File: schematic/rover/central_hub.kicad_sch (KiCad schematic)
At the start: 8 parts, among them U1 Pico

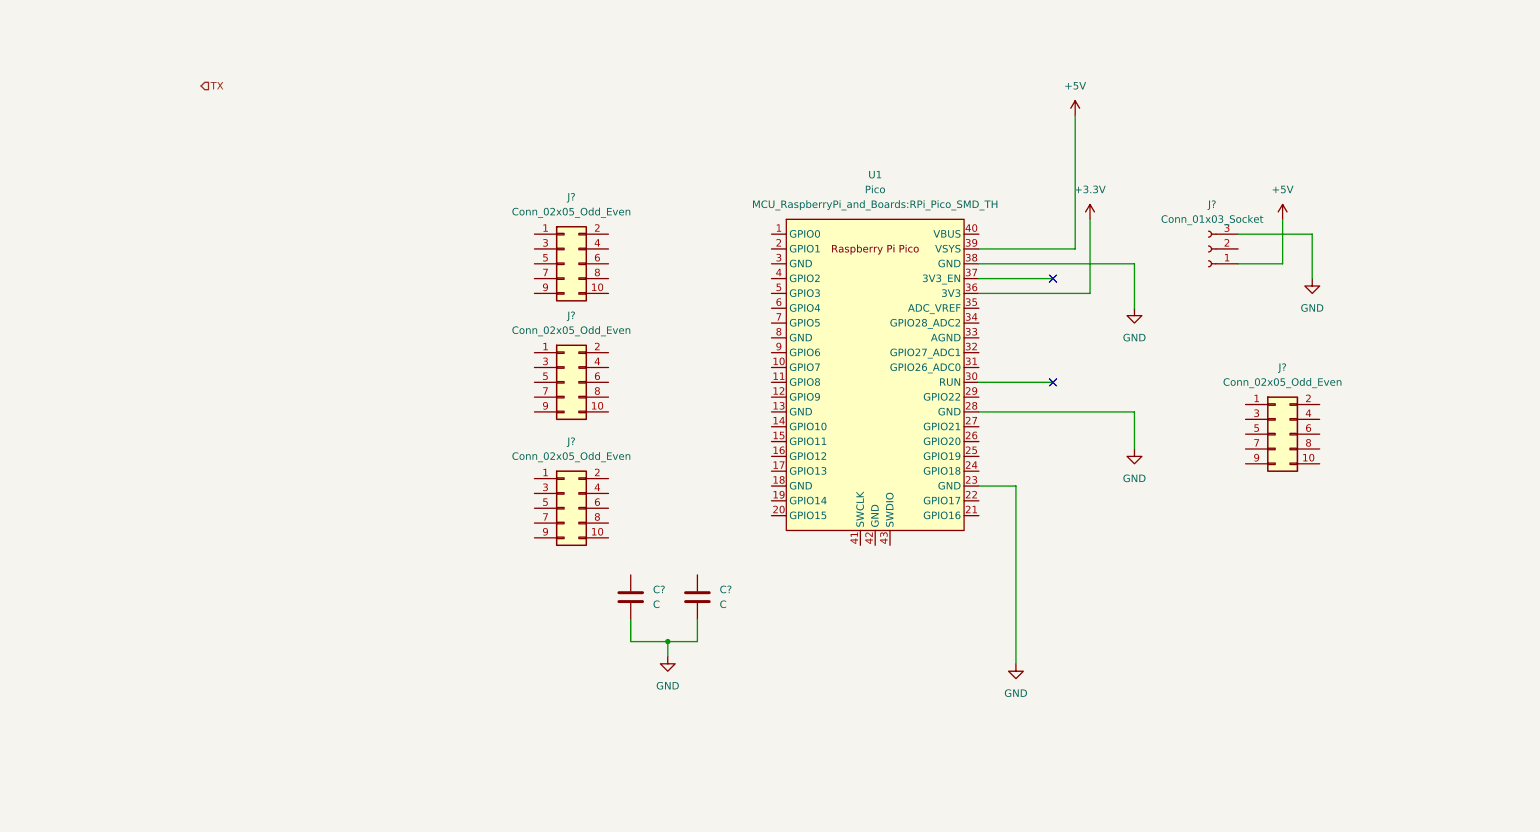
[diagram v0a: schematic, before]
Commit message: Complete Central Hub schematic
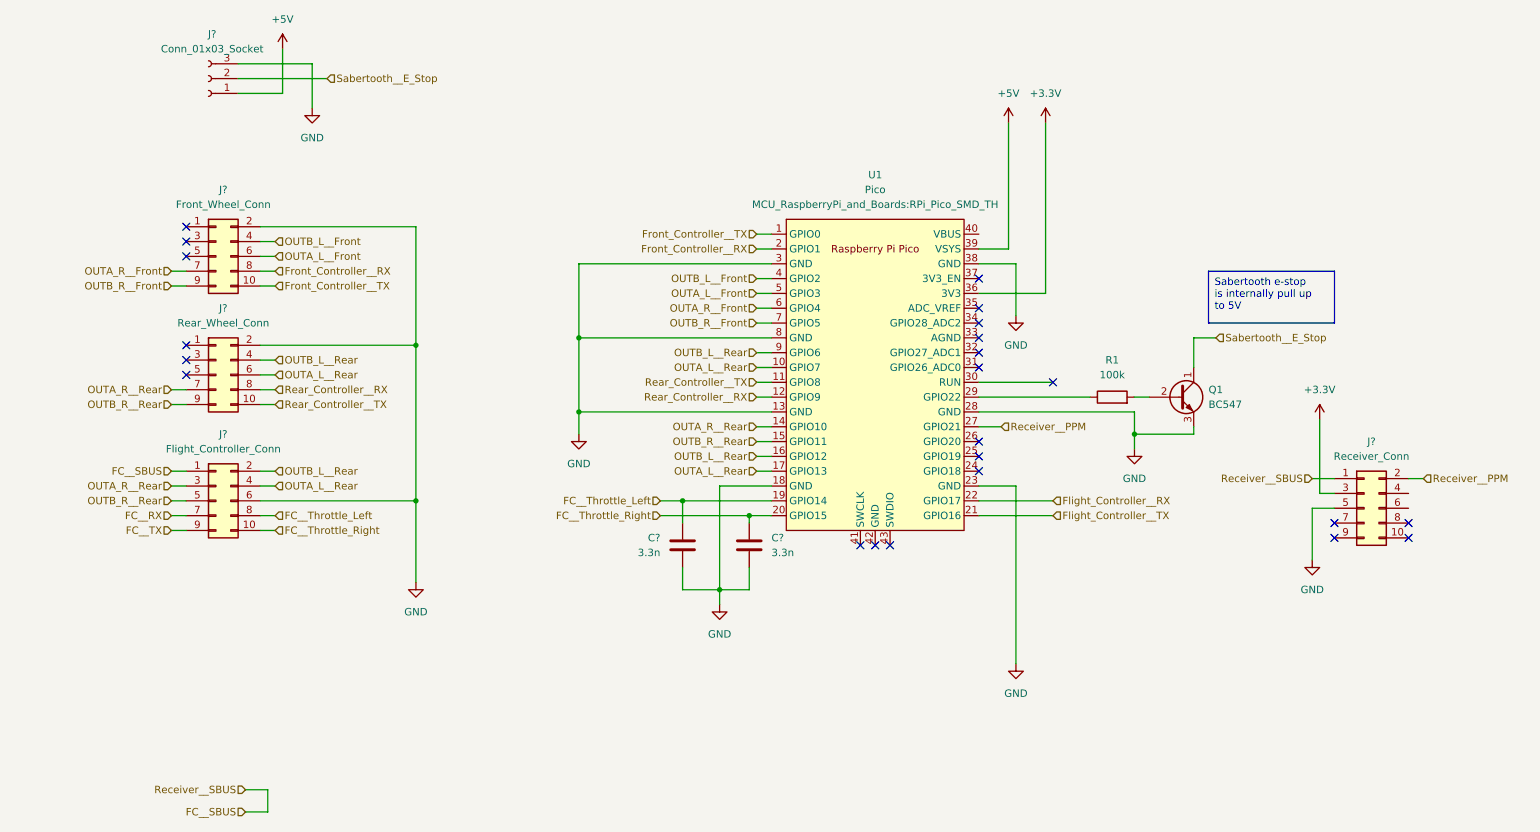
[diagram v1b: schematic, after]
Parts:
- removed C?: C, Capacitor_THT:C_Disc_D7.5mm_W5.0mm_P7.50mm, symbol Device:C
- added C?: 3.3n, Capacitor_THT:C_Disc_D5.0mm_W2.5mm_P5.00mm, symbol Device:C
- added Q1: BC547, Package_TO_SOT_THT:TO-92_Inline, symbol Transistor_BJT:BC547
- added R1: 100k, Resistor_THT:R_Axial_DIN0207_L6.3mm_D2.5mm_P5.08mm_Vertical, symbol Device:R
- C?: value C -> 3.3n; footprint Capacitor_THT:C_Disc_D7.5mm_W5.0mm_P7.50mm -> Capacitor_THT:C_Disc_D5.0mm_W2.5mm_P5.00mm
- J?: value Conn_02x05_Odd_Even -> Receiver_Conn
- J?: value Conn_02x05_Odd_Even -> Rear_Wheel_Conn
- J?: value Conn_02x05_Odd_Even -> Front_Wheel_Conn
- J?: value Conn_02x05_Odd_Even -> Flight_Controller_Conn
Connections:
- net +3.3V: now also J?.3 (Pin_3)
- net GND: now also J?.2 (Pin_2), J?.2 (Pin_2), J?.5 (Pin_5), J?.6 (Pin_6), U1.13 (GND), U1.18 (GND), U1.3 (GND), U1.8 (GND), C?.2, Q1.3 (E)
- net FC__SBUS: now reaches J?.1 (Pin_1)
- net FC__SBUS: now also J?.1 (Pin_1)
- net Receiver__PPM: now reaches J?.2 (Pin_2)
- net Receiver__PPM: now also U1.27 (GPIO21)
- net Sabertooth__E_Stop: now reaches J?.2 (Pin_2)
- net Sabertooth__E_Stop: now also Q1.1 (C)
- net Front_Controller__TX: now reaches U1.1 (GPIO0)
- net Front_Controller__TX: now also J?.10 (Pin_10)
- net OUTA_L__Rear: now reaches U1.10 (GPIO7)
- net OUTA_L__Rear: now also J?.4 (Pin_4), J?.6 (Pin_6), U1.17 (GPIO13)
- net Rear_Controller__TX: now reaches U1.11 (GPIO8)
- net Rear_Controller__TX: now also J?.10 (Pin_10)
- net Rear_Controller__RX: now reaches U1.12 (GPIO9)
- net Rear_Controller__RX: now also J?.8 (Pin_8)
- net OUTA_R__Rear: now reaches U1.14 (GPIO10)
- net OUTA_R__Rear: now also J?.3 (Pin_3), J?.7 (Pin_7)
- net OUTB_R__Rear: now reaches U1.15 (GPIO11)
- net OUTB_R__Rear: now also J?.5 (Pin_5), J?.9 (Pin_9)
- net OUTB_L__Rear: now reaches U1.16 (GPIO12)
- net OUTB_L__Rear: now also J?.2 (Pin_2), J?.4 (Pin_4), U1.9 (GPIO6)
- net FC__Throttle_Left: now reaches U1.19 (GPIO14)
- net FC__Throttle_Left: now also C?.1, J?.8 (Pin_8)
- net Front_Controller__RX: now reaches U1.2 (GPIO1)
- net Front_Controller__RX: now also J?.8 (Pin_8)
- net FC__Throttle_Right: now reaches U1.20 (GPIO15)
- net FC__Throttle_Right: now also J?.10 (Pin_10), C?.1
- net Flight_Controller__TX: now reaches U1.21 (GPIO16)
- net Flight_Controller__RX: now reaches U1.22 (GPIO17)
- net at U1.29 (GPIO22): now also R1.1
- net OUTB_L__Front: now reaches U1.4 (GPIO2)
- net OUTB_L__Front: now also J?.4 (Pin_4)
- net OUTA_L__Front: now reaches U1.5 (GPIO3)
- net OUTA_L__Front: now also J?.6 (Pin_6)
- net OUTA_R__Front: now reaches U1.6 (GPIO4)
- net OUTA_R__Front: now also J?.7 (Pin_7)
- net OUTB_R__Front: now reaches U1.7 (GPIO5)
- net OUTB_R__Front: now also J?.9 (Pin_9)
- net FC__RX: now reaches J?.7 (Pin_7)
- net FC__TX: now reaches J?.9 (Pin_9)
- new net: Q1.2 (B), R1.2
- no-connect marks 2 -> 23
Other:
- moved on the sheet: C?, J?

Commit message: Update connection between picos
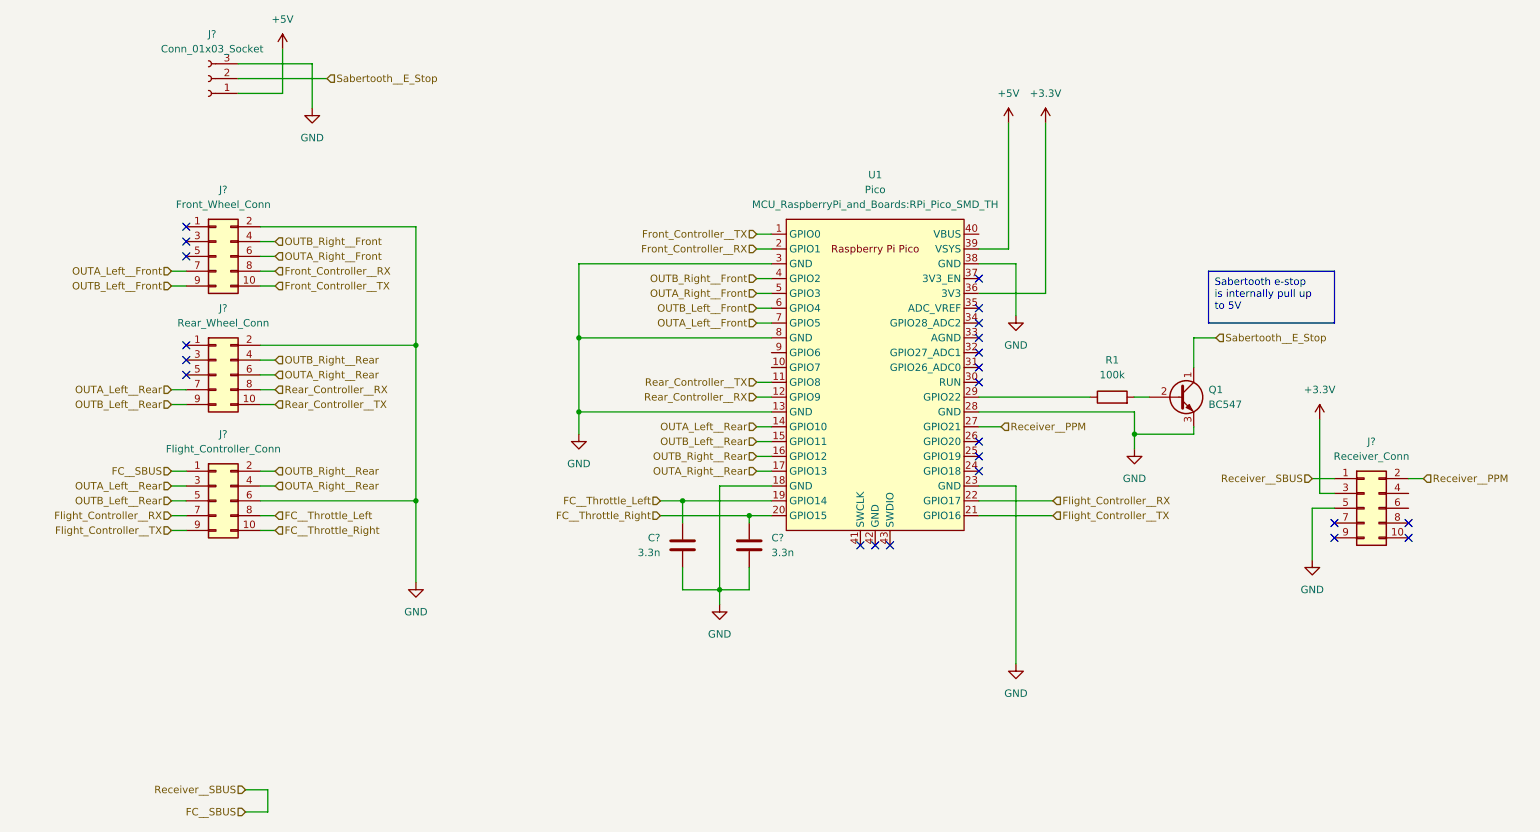
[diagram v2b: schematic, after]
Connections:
- net FC__RX is gone; now on net Flight_Controller__RX: J?.7 (Pin_7)
- net FC__TX is gone; now on net Flight_Controller__TX: J?.9 (Pin_9)
- net OUTA_L__Front renamed OUTA_Right__Front
- net OUTA_L__Rear renamed OUTA_Right__Rear
- net OUTA_Right__Rear: no longer U1.10 (GPIO7)
- net OUTA_R__Front renamed OUTA_Left__Front
- net OUTA_Left__Front: now also U1.7 (GPIO5); no longer U1.6 (GPIO4)
- net OUTA_R__Rear renamed OUTA_Left__Rear
- net OUTB_L__Front renamed OUTB_Right__Front
- net OUTB_L__Rear renamed OUTB_Right__Rear
- net OUTB_Right__Rear: no longer U1.9 (GPIO6)
- net OUTB_R__Front renamed OUTB_Left__Front
- net OUTB_Left__Front: now also U1.6 (GPIO4); no longer U1.7 (GPIO5)
- net OUTB_R__Rear renamed OUTB_Left__Rear
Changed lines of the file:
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@@
   (no_connect (at 238.76 114.3))
   (no_connect (at 41.91 86.36))
-  (no_connect (at 190.5 87.63))
+  (no_connect (at 177.8 87.63))
   (no_connect (at 177.8 77.47))
   (no_connect (at 177.8 85.09))
@@
     (stroke (width 0) (type default))
   )
-  (wire (pts (xy 190.5 87.63) (xy 177.8 87.63))
-    (stroke (width 0) (type default))
-  )
   (wire (pts (xy 204.47 92.71) (xy 204.47 96.52))
     (stroke (width 0) (type default))
@@
     (stroke (width 0) (type default))
   )
-  (wire (pts (xy 139.7 85.09) (xy 142.24 85.09))
-    (stroke (width 0) (type default))
-  )
   (wire (pts (xy 109.22 92.71) (xy 109.22 96.52))
     (stroke (width 0) (type default))
@@
   )
   (wire (pts (xy 138.43 110.49) (xy 138.43 111.76))
-    (stroke (width 0) (type default))
-  )
-  (wire (pts (xy 139.7 82.55) (xy 142.24 82.55))
     (stroke (width 0) (type default))
   )
@@
     (effects (font (size 1.27 1.27)) (justify left top))
   )
-  (hierarchical_label "OUTA_R__Rear" (shape input) (at 139.7 95.25 180) (fields_autoplaced)
-    (effects (font (size 1.27 1.27)) (justify right))
-  )
-  (hierarchical_label "OUTA_L__Front" (shape input) (at 139.7 72.39 180) (fields_autoplaced)
+  (hierarchical_label "OUTA_Left__Rear" (shape input) (at 139.7 95.25 180) (fields_autoplaced)
+    (effects (font (size 1.27 1.27)) (justify right))
+  )
+  (hierarchical_label "OUTA_Right__Front" (shape input) (at 139.7 72.39 180) (fields_autoplaced)
     (effects (font (size 1.27 1.27)) (justify right))
   )
@@
     (effects (font (size 1.27 1.27)) (justify left))
   )
-  (hierarchical_label "OUTB_L__Rear" (shape input) (at 139.7 82.55 180) (fields_autoplaced)
-    (effects (font (size 1.27 1.27)) (justify right))
-  )
-  (hierarchical_label "OUTB_R__Rear" (shape input) (at 39.37 107.95 180) (fields_autoplaced)
+  (hierarchical_label "OUTB_Left__Rear" (shape input) (at 39.37 107.95 180) (fields_autoplaced)
     (effects (font (size 1.27 1.27)) (justify right))
   )
@@
     (effects (font (size 1.27 1.27)) (justify left))
   )
-  (hierarchical_label "OUTA_R__Front" (shape input) (at 39.37 68.58 180) (fields_autoplaced)
-    (effects (font (size 1.27 1.27)) (justify right))
-  )
-  (hierarchical_label "OUTB_R__Front" (shape input) (at 39.37 71.12 180) (fields_autoplaced)
+  (hierarchical_label "OUTA_Left__Front" (shape input) (at 39.37 68.58 180) (fields_autoplaced)
+    (effects (font (size 1.27 1.27)) (justify right))
+  )
+  (hierarchical_label "OUTB_Left__Front" (shape input) (at 39.37 71.12 180) (fields_autoplaced)
     (effects (font (size 1.27 1.27)) (justify right))
   )
@@
     (effects (font (size 1.27 1.27)) (justify left))
   )
-  (hierarchical_label "OUTB_L__Front" (shape input) (at 139.7 69.85 180) (fields_autoplaced)
+  (hierarchical_label "OUTB_Right__Front" (shape input) (at 139.7 69.85 180) (fields_autoplaced)
     (effects (font (size 1.27 1.27)) (justify right))
   )
@@
     (effects (font (size 1.27 1.27)) (justify left))
   )
-  (hierarchical_label "OUTB_L__Rear" (shape input) (at 57.15 102.87 0) (fields_autoplaced)
+  (hierarchical_label "OUTB_Right__Rear" (shape input) (at 57.15 102.87 0) (fields_autoplaced)
     (effects (font (size 1.27 1.27)) (justify left))
   )
@@
     (effects (font (size 1.27 1.27)) (justify right))
   )
-  (hierarchical_label "OUTB_L__Front" (shape input) (at 57.15 63.5 0) (fields_autoplaced)
-    (effects (font (size 1.27 1.27)) (justify left))
-  )
-  (hierarchical_label "OUTA_L__Rear" (shape input) (at 139.7 85.09 180) (fields_autoplaced)
-    (effects (font (size 1.27 1.27)) (justify right))
-  )
-  (hierarchical_label "OUTA_R__Rear" (shape input) (at 39.37 88.9 180) (fields_autoplaced)
+  (hierarchical_label "OUTB_Right__Front" (shape input) (at 57.15 63.5 0) (fields_autoplaced)
+    (effects (font (size 1.27 1.27)) (justify left))
+  )
+  (hierarchical_label "OUTA_Left__Rear" (shape input) (at 39.37 88.9 180) (fields_autoplaced)
     (effects (font (size 1.27 1.27)) (justify right))
   )
@@
     (effects (font (size 1.27 1.27)) (justify left))
   )
-  (hierarchical_label "OUTB_R__Rear" (shape input) (at 139.7 97.79 180) (fields_autoplaced)
+  (hierarchical_label "OUTB_Left__Rear" (shape input) (at 139.7 97.79 180) (fields_autoplaced)
+    (effects (font (size 1.27 1.27)) (justify right))
+  )
+  (hierarchical_label "OUTA_Left__Front" (shape input) (at 139.7 77.47 180) (fields_autoplaced)
     (effects (font (size 1.27 1.27)) (justify right))
   )
@@
     (effects (font (size 1.27 1.27)) (justify left))
   )
-  (hierarchical_label "OUTA_R__Rear" (shape input) (at 39.37 105.41 180) (fields_autoplaced)
-    (effects (font (size 1.27 1.27)) (justify right))
-  )
-  (hierarchical_label "OUTB_R__Front" (shape input) (at 139.7 77.47 180) (fields_autoplaced)
-    (effects (font (size 1.27 1.27)) (justify right))
-  )
-  (hierarchical_label "OUTA_R__Front" (shape input) (at 139.7 74.93 180) (fields_autoplaced)
-    (effects (font (size 1.27 1.27)) (justify right))
-  )
-  (hierarchical_label "FC__RX" (shape input) (at 39.37 110.49 180) (fields_autoplaced)
-    (effects (font (size 1.27 1.27)) (justify right))
-  )
-  (hierarchical_label "OUTB_R__Rear" (shape input) (at 39.37 91.44 180) (fields_autoplaced)
+  (hierarchical_label "OUTA_Left__Rear" (shape input) (at 39.37 105.41 180) (fields_autoplaced)
+    (effects (font (size 1.27 1.27)) (justify right))
+  )
+  (hierarchical_label "Flight_Controller__RX" (shape input) (at 39.37 110.49 180) (fields_autoplaced)
+    (effects (font (size 1.27 1.27)) (justify right))
+  )
+  (hierarchical_label "OUTB_Left__Rear" (shape input) (at 39.37 91.44 180) (fields_autoplaced)
     (effects (font (size 1.27 1.27)) (justify right))
   )
@@
     (effects (font (size 1.27 1.27)) (justify right))
   )
-  (hierarchical_label "OUTA_L__Rear" (shape input) (at 139.7 102.87 180) (fields_autoplaced)
+  (hierarchical_label "OUTA_Right__Rear" (shape input) (at 139.7 102.87 180) (fields_autoplaced)
     (effects (font (size 1.27 1.27)) (justify right))
   )
@@
     (effects (font (size 1.27 1.27)) (justify left))
   )
-  (hierarchical_label "FC__TX" (shape input) (at 39.37 113.03 180) (fields_autoplaced)
+  (hierarchical_label "OUTB_Left__Front" (shape input) (at 139.7 74.93 180) (fields_autoplaced)
+    (effects (font (size 1.27 1.27)) (justify right))
+  )
+  (hierarchical_label "Flight_Controller__TX" (shape input) (at 39.37 113.03 180) (fields_autoplaced)
     (effects (font (size 1.27 1.27)) (justify right))
   )
@@
     (effects (font (size 1.27 1.27)) (justify right))
   )
-  (hierarchical_label "OUTB_L__Rear" (shape input) (at 57.15 83.82 0) (fields_autoplaced)
-    (effects (font (size 1.27 1.27)) (justify left))
-  )
-  (hierarchical_label "OUTB_L__Rear" (shape input) (at 139.7 100.33 180) (fields_autoplaced)
+  (hierarchical_label "OUTB_Right__Rear" (shape input) (at 57.15 83.82 0) (fields_autoplaced)
+    (effects (font (size 1.27 1.27)) (justify left))
+  )
+  (hierarchical_label "OUTB_Right__Rear" (shape input) (at 139.7 100.33 180) (fields_autoplaced)
     (effects (font (size 1.27 1.27)) (justify right))
   )
@@
     (effects (font (size 1.27 1.27)) (justify left))
   )
-  (hierarchical_label "OUTA_L__Rear" (shape input) (at 57.15 86.36 0) (fields_autoplaced)
-    (effects (font (size 1.27 1.27)) (justify left))
-  )
-  (hierarchical_label "OUTA_L__Rear" (shape input) (at 57.15 105.41 0) (fields_autoplaced)
-    (effects (font (size 1.27 1.27)) (justify left))
-  )
-  (hierarchical_label "OUTA_L__Front" (shape input) (at 57.15 66.04 0) (fields_autoplaced)
-    (effects (font (size 1.27 1.27)) (justify left))
-  )
+  (hierarchical_label "OUTA_Right__Rear" (shape input) (at 57.15 86.36 0) (fields_autoplaced)
+    (effects (font (size 1.27 1.27)) (justify left))
+  )
+  (hierarchical_label "OUTA_Right__Rear" (shape input) (at 57.15 105.41 0) (fields_autoplaced)
+    (effects (font (size 1.27 1.27)) (justify left))
+  )
+  (hierarchical_label "OUTA_Right__Front" (shape input) (at 57.15 66.04 0) (fields_autoplaced)
+    (effects (font (size 1.27 1.27)) (justify left))
+  )
